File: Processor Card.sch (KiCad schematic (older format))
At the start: 31 parts, among them J1 Serial Port, J2 Conn_02x20_Odd_Even, U1 74LS32, U2 74LS04, U3 28C256 / 62256, U4 74LS73, U5 28C256 / 62256, U6 CDP1802/1806, U7 74LS373, U8 74LS138

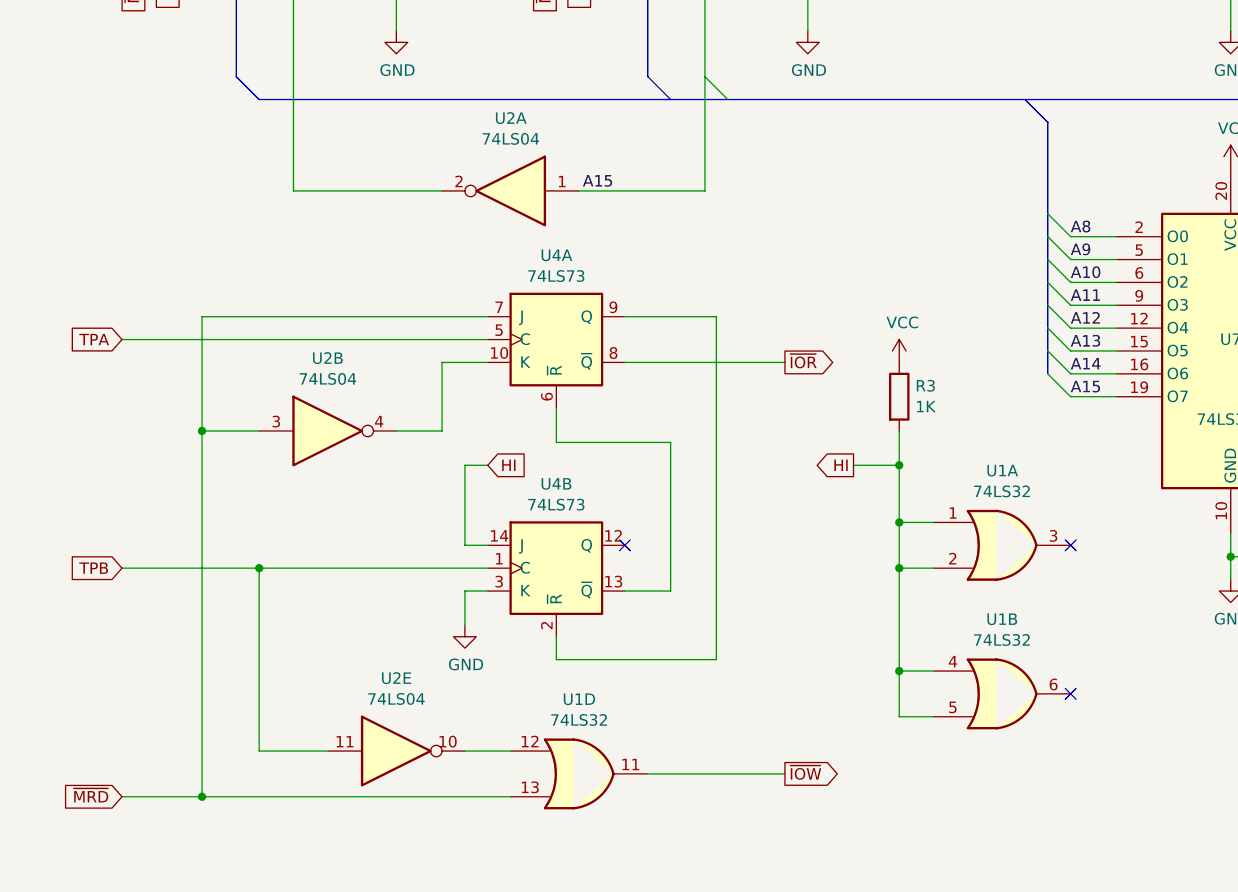
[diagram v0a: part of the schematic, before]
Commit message: Added Gate Delay to IO Decode
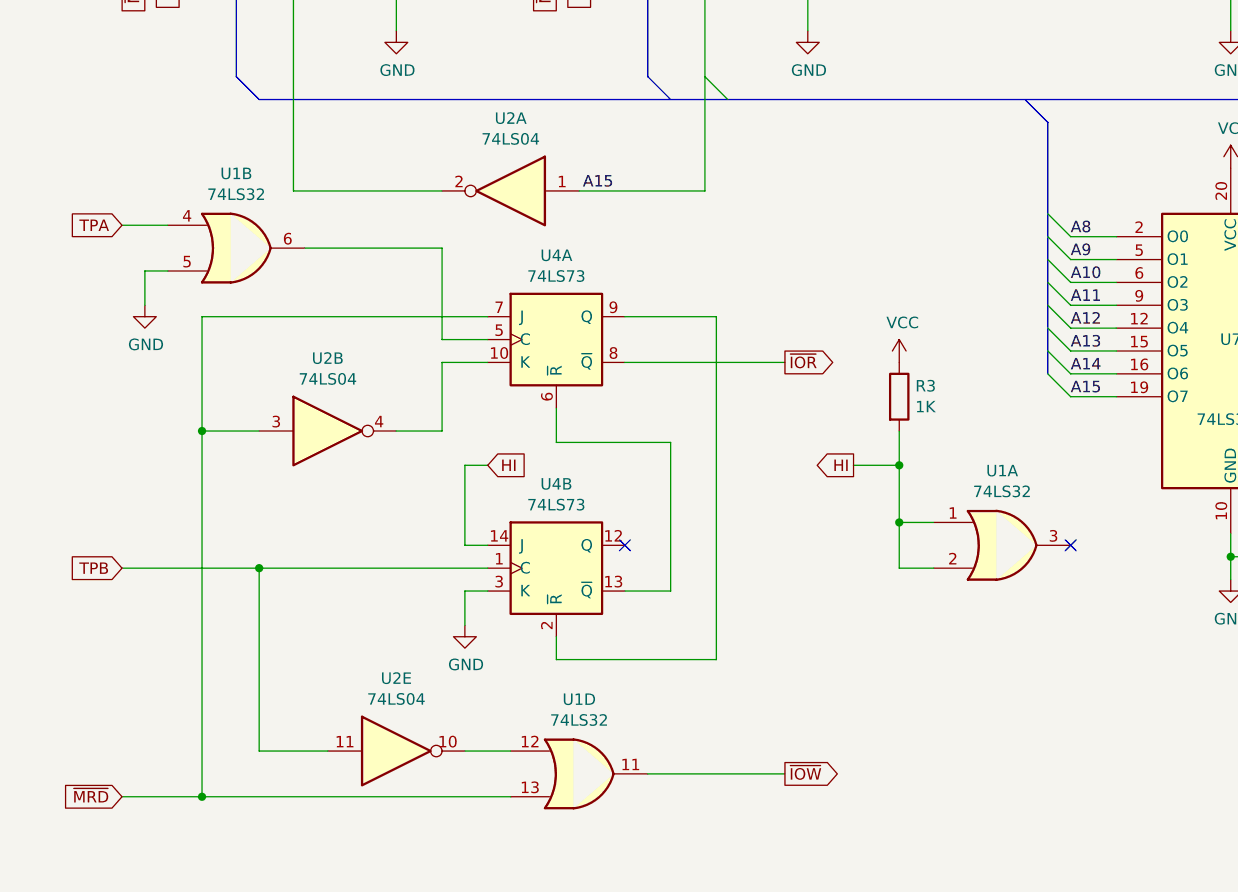
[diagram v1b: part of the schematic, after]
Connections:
- net GND: now also U1.5
- net HI: no longer U1.4, U1.5
- net TPA: now also U1.4; no longer U4.5 (C)
- net at U1.6: now also U4.5 (C)
- no-connect marks 9 -> 8
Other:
- moved on the sheet: U1B
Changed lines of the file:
@@
 Title "Cosmac Elf"
 Date "2020-12-06"
-Rev "1"
+Rev "2"
 Comp ""
 Comment1 "Processor Card"
@@
 	1    0    0    -1
 $EndComp
-Text GLabel 1000 5400 0    50   Input ~ 0
+Text GLabel 1000 4900 0    50   Input ~ 0
 TPA
 Text GLabel 1000 6400 0    50   Input ~ 0
@@
 L 74xx:74LS32 U1
 U 2 1 604DB09A
-P 4850 6950
-F 0 "U1" H 4850 7275 50  0000 C CNN
-F 1 "74LS32" H 4850 7184 50  0000 C CNN
-F 2 "Package_DIP:DIP-14_W7.62mm" H 4850 6950 50  0001 C CNN
-F 3 "http://www.ti.com/lit/gpn/sn74LS32" H 4850 6950 50  0001 C CNN
-	2    4850 6950
+P 1500 5000
+F 0 "U1" H 1500 5325 50  0000 C CNN
+F 1 "74LS32" H 1500 5234 50  0000 C CNN
+F 2 "Package_DIP:DIP-14_W7.62mm" H 1500 5000 50  0001 C CNN
+F 3 "http://www.ti.com/lit/gpn/sn74LS32" H 1500 5000 50  0001 C CNN
+	2    1500 5000
 	1    0    0    -1
 $EndComp
@@
 $EndComp
 Wire Wire Line
-	2600 5400 1000 5400
-Wire Wire Line
-	4550 7050 4400 7050
-Wire Wire Line
-	4400 7050 4400 6850
-Connection ~ 4400 6400
-Wire Wire Line
-	4550 6850 4400 6850
-Connection ~ 4400 6850
-Wire Wire Line
-	4400 6850 4400 6400
-NoConn ~ 5150 6950
+	2600 5400 2400 5400
+Wire Wire Line
+	2400 5400 2400 5000
+Wire Wire Line
+	2400 5000 1800 5000
+Wire Wire Line
+	1000 4900 1200 4900
+Wire Wire Line
+	1200 5100 1100 5100
+Wire Wire Line
+	1100 5100 1100 5250
+$Comp
+L power:GND #PWR0103
+U 1 1 61974A32
+P 1100 5250
+F 0 "#PWR0103" H 1100 5000 50  0001 C CNN
+F 1 "GND" H 1105 5077 50  0000 C CNN
+F 2 "" H 1100 5250 50  0001 C CNN
+F 3 "" H 1100 5250 50  0001 C CNN
+	1    1100 5250
+	1    0    0    -1
+$EndComp
 Wire Wire Line
 	3550 3650 3550 4750

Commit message: Sync
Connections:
- net HI: no longer U1.1, U1.2
- net at U4.5 (C): now also U1.3; no longer U1.6
- new net: U1.1, U1.2, U1.6
- no-connect marks 8 -> 7
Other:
- moved on the sheet: R3, U1A, U1B, U1D, U2B, U2E, U4A, U4B
